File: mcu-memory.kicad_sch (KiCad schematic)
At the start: 1 part, among them U2 AT25SF081-SSHD-X

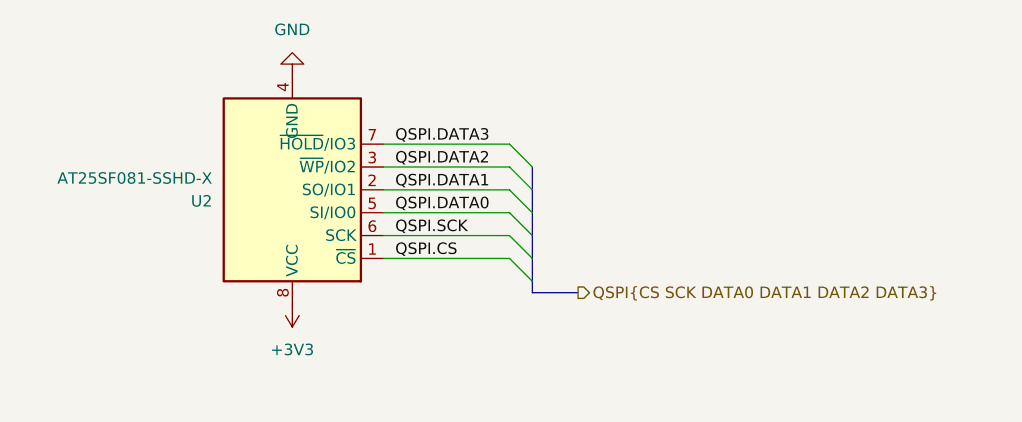
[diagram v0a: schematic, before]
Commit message: Adding symbols information
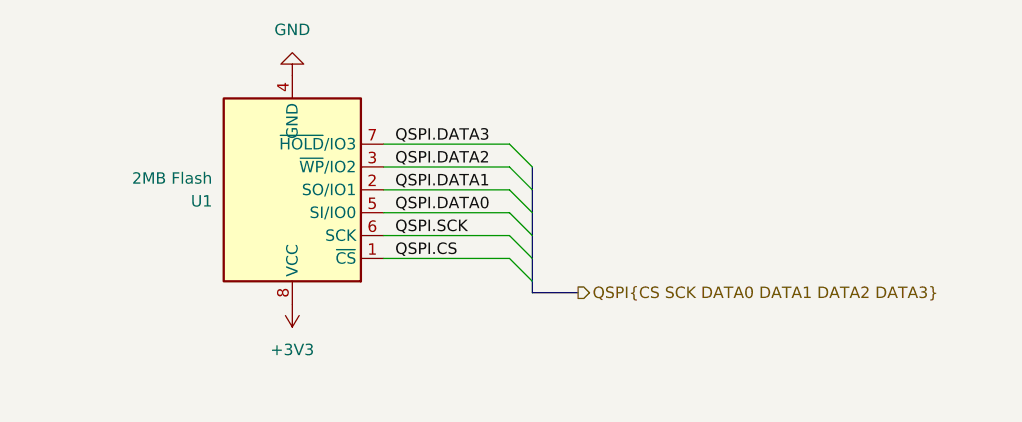
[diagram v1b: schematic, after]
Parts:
- U1: renamed from U2; value AT25SF081-SSHD-X -> 2MB Flash; Mfr (none) -> GigaDevice Semiconductor (HK) Limited; Mfr P/N (none) -> GD25Q16ETIGR; Supplier_1 (none) -> Digikey; Supplier_1 P/N (none) -> 1970-GD25Q16ETIGRCT-ND; Supplier_1 Price @ Qty (none) -> 0.59060; Supplier_1 Unit Price (none) -> 0.74
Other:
- company: (none) -> catbranchman
- title: (none) -> MCU - Memory
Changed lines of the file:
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@@
 	(generator_version "8.0")
 	(paper "A4")
+	(title_block
+		(title "MCU - Memory")
+		(rev "0.1")
+		(company "catbranchman")
+		(comment 1 "Electrical Engineering Department")
+		(comment 2 "EE 156 / Stanford University")
+		(comment 3 "Flight Club, W6YX, Endurance")
+	)
 	(bus_entry
 		(at 163.83 92.71)
@@
 		(dnp no)
 		(fields_autoplaced yes)
-		(property "Reference" "U2"
+		(property "Reference" "U1"
 			(at 130.81 99.0601 0)
 			(effects
@@
 			)
 		)
-		(property "Value" "AT25SF081-SSHD-X"
+		(property "Value" "2MB Flash"
 			(at 130.81 96.5201 0)
 			(effects
@@
 			)
 		)
-		(property "Datasheet" "https://www.adestotech.com/wp-content/uploads/DS-AT25SF081_045.pdf"
-			(at 139.7 97.79 0)
-			(effects
-				(font
-					(size 1.27 1.27)
-				)
-				(hide yes)
-			)
-		)
-		(property "Description" "8-Mbit, 2.5V Minimum SPI Serial Flash Memory with Dual-I/O and Quad-I/O Support, SOIC-8"
+		(property "Datasheet" "https://www.gigadevice.com.cn/Public/Uploads/uploadfile/files/20220714/DS-00473-GD25Q16E-Rev1.2.pdf"
+			(at 139.7 97.79 0)
+			(effects
+				(font
+					(size 1.27 1.27)
+				)
+				(hide yes)
+			)
+		)
+		(property "Description" "FLASH - NOR Memory IC 16Mbit SPI - Quad 1/0 133 MHz 7 ns 8-USON (2x3)"
+			(at 139.7 97.79 0)
+			(effects
+				(font
+					(size 1.27 1.27)
+				)
+				(hide yes)
+			)
+		)
+		(property "Mfr" "GigaDevice Semiconductor (HK) Limited"
+			(at 139.7 97.79 0)
+			(effects
+				(font
+					(size 1.27 1.27)
+				)
+				(hide yes)
+			)
+		)
+		(property "Mfr P/N" "GD25Q16ETIGR"
+			(at 139.7 97.79 0)
+			(effects
+				(font
+					(size 1.27 1.27)
+				)
+				(hide yes)
+			)
+		)
+		(property "Supplier_1" "Digikey"
+			(at 139.7 97.79 0)
+			(effects
+				(font
+					(size 1.27 1.27)
+				)
+				(hide yes)
+			)
+		)
+		(property "Supplier_1 P/N" "1970-GD25Q16ETIGRCT-ND"
+			(at 139.7 97.79 0)
+			(effects
+				(font
+					(size 1.27 1.27)
+				)
+				(hide yes)
+			)
+		)
+		(property "Supplier_1 Unit Price" "0.74"
+			(at 139.7 97.79 0)
+			(effects
+				(font
+					(size 1.27 1.27)
+				)
+				(hide yes)
+			)
+		)
+		(property "Supplier_1 Price @ Qty" "0.59060"
+			(at 139.7 97.79 0)
+			(effects
+				(font
+					(size 1.27 1.27)
+				)
+				(hide yes)
+			)
+		)
+		(property "Supplier_2" ""
+			(at 139.7 97.79 0)
+			(effects
+				(font
+					(size 1.27 1.27)
+				)
+				(hide yes)
+			)
+		)
+		(property "Supplier_2 P/N" ""
+			(at 139.7 97.79 0)
+			(effects
+				(font
+					(size 1.27 1.27)
+				)
+				(hide yes)
+			)
+		)
+		(property "Supplier_2 Unit Price" ""
+			(at 139.7 97.79 0)
+			(effects
+				(font
+					(size 1.27 1.27)
+				)
+				(hide yes)
+			)
+		)
+		(property "Supplier_2 Price @ Qty" ""
 			(at 139.7 97.79 0)
 			(effects
@@
 			(project ""
 				(path "/1c59de6a-87fe-4223-8898-4b0383164a31/2af03a7b-eb0a-4c9d-bb49-ade4165c64a7"
-					(reference "U2")
+					(reference "U1")
 					(unit 1)
 				)

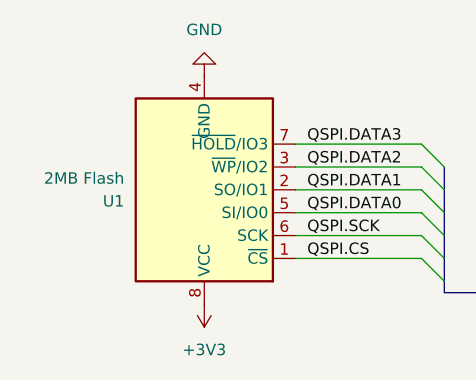
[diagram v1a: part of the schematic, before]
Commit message: Fixing footprint imports
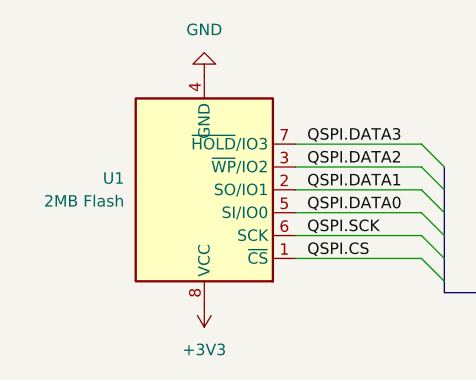
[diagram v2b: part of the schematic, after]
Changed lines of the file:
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@@
 		(fields_autoplaced yes)
 		(property "Reference" "U1"
-			(at 130.81 99.0601 0)
+			(at 130.81 96.5199 0)
 			(effects
 				(font
@@
 		)
 		(property "Value" "2MB Flash"
-			(at 130.81 96.5201 0)
+			(at 130.81 99.0599 0)
 			(effects
 				(font

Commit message: Working on layout still
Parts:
- added R5: 10K, Resistor_SMD:R_0603_1608Metric, symbol Device:R
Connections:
- net +3V3: now also R5.1
- net QSPI.CS: now also R5.2
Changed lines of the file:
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@@
 		(comment 3 "Flight Club, W6YX, Endurance")
+	)
+	(junction
+		(at 161.29 105.41)
+		(diameter 0)
+		(color 0 0 0 0)
 	)
 	(bus_entry
@@
 		)
 	)
+	(wire
+		(pts
+			(xy 161.29 105.41) (xy 163.83 105.41)
+		)
+		(stroke
+			(width 0)
+			(type default)
+		)
+	)
 	(bus
 		(pts
@@
 	(wire
 		(pts
-			(xy 149.86 105.41) (xy 163.83 105.41)
+			(xy 149.86 105.41) (xy 161.29 105.41)
 		)
 		(stroke
@@
 			)
 			(justify left)
+		)
+	)
+	(symbol
+		(lib_id "Device:R")
+		(at 161.29 109.22 180)
+		(unit 1)
+		(exclude_from_sim no)
+		(in_bom yes)
+		(on_board yes)
+		(dnp no)
+		(property "Reference" "R5"
+			(at 159.004 108.204 90)
+			(effects
+				(font
+					(size 1.27 1.27)
+				)
+				(justify left)
+			)
+		)
+		(property "Value" "10K"
+			(at 161.29 107.188 90)
+			(effects
+				(font
+					(size 1.27 1.27)
+					(thickness 0.254)
+					(bold yes)
+				)
+				(justify left)
+			)
+		)
+		(property "Footprint" "Resistor_SMD:R_0603_1608Metric"
+			(at 163.068 109.22 90)
+			(effects
+				(font
+					(size 1.27 1.27)
+				)
+				(hide yes)
+			)
+		)
+		(property "Datasheet" "https://www.seielect.com/catalog/sei-rncp.pdf"
+			(at 161.29 109.22 0)
+			(effects
+				(font
+					(size 1.27 1.27)
+				)
+				(hide yes)
+			)
+		)
+		(property "Description" "10 kOhms 1% 0.125W, 1/8W Chip Resistor 0603 (1608 Metric) Anti-Sulfur Thin Film"
+			(at 161.29 109.22 0)
+			(effects
+				(font
+					(size 1.27 1.27)
+				)
+				(hide yes)
+			)
+		)
+		(property "Mfr" "Stackpole Electronics Inc"
+			(at 161.29 109.22 0)
+			(effects
+				(font
+					(size 1.27 1.27)
+				)
+				(hide yes)
+			)
+		)
+		(property "Mfr P/N" "RNCP0603FTD10K0"
+			(at 161.29 109.22 0)
+			(effects
+				(font
+					(size 1.27 1.27)
+				)
+				(hide yes)
+			)
+		)
+		(property "Supplier_1" "Digikey"
+			(at 161.29 109.22 0)
+			(effects
+				(font
+					(size 1.27 1.27)
+				)
+				(hide yes)
+			)
+		)
+		(property "Supplier_1 P/N" "RNCP0603FTD10K0CT-ND"
+			(at 161.29 109.22 0)
+			(effects
+				(font
+					(size 1.27 1.27)
+				)
+				(hide yes)
+			)
+		)
+		(property "Supplier_1 Unit Price" "0.10"
+			(at 161.29 109.22 0)
+			(effects
+				(font
+					(size 1.27 1.27)
+				)
+				(hide yes)
+			)
+		)
+		(property "Supplier_1 Price @ Qty" "0.0170"
+			(at 161.29 109.22 0)
+			(effects
+				(font
+					(size 1.27 1.27)
+				)
+				(hide yes)
+			)
+		)
+		(property "Supplier_2" ""
+			(at 161.29 109.22 0)
+			(effects
+				(font
+					(size 1.27 1.27)
+				)
+				(hide yes)
+			)
+		)
+		(property "Supplier_2 P/N" ""
+			(at 161.29 109.22 0)
+			(effects
+				(font
+					(size 1.27 1.27)
+				)
+				(hide yes)
+			)
+		)
+		(property "Supplier_2 Unit Price" ""
+			(at 161.29 109.22 0)
+			(effects
+				(font
+					(size 1.27 1.27)
+				)
+				(hide yes)
+			)
+		)
+		(property "Supplier_2 Price @ Qty" ""
+			(at 161.29 109.22 0)
+			(effects
+				(font
+					(size 1.27 1.27)
+				)
+				(hide yes)
+			)
+		)
+		(pin "2"
+		)
+		(pin "1"
+		)
+		(instances
+			(project "roamer"
+				(path "/1c59de6a-87fe-4223-8898-4b0383164a31/2af03a7b-eb0a-4c9d-bb49-ade4165c64a7"
+					(reference "R5")
+					(unit 1)
+				)
+			)
 		)
 	)
@@
 					(unit 1)
 				)
+			)
+		)
+	)
+	(symbol
+		(lib_id "power:+3V3")
+		(at 161.29 113.03 180)
+		(unit 1)
+		(exclude_from_sim no)
+		(in_bom yes)
+		(on_board yes)
+		(dnp no)
+		(property "Reference" "#PWR041"
+			(at 161.29 109.22 0)
+			(effects
+				(font
+					(size 1.27 1.27)
+				)
+				(hide yes)
+			)
+		)
+		(property "Value" "+3V3"
+			(at 161.29 118.618 90)
+			(effects
+				(font
+					(size 1.27 1.27)
+				)
+			)
+		)
+		(property "Footprint" ""
+			(at 161.29 113.03 0)
+			(effects
+				(font
+					(size 1.27 1.27)
+				)
+				(hide yes)
+			)
+		)
+		(property "Datasheet" ""
+			(at 161.29 113.03 0)
+			(effects
+				(font
+					(size 1.27 1.27)
+				)
+				(hide yes)
+			)
+		)
+		(property "Description" "Power symbol creates a global label with name \"+3V3\""
+			(at 161.29 113.03 0)
+			(effects
+				(font
+					(size 1.27 1.27)
+				)
+				(hide yes)
+			)
+		)
+		(pin "1"
+		)
+		(instances
+			(project "roamer"
+				(path "/1c59de6a-87fe-4223-8898-4b0383164a31/2af03a7b-eb0a-4c9d-bb49-ade4165c64a7"
+					(reference "#PWR041")
+					(unit 1)
+				)
